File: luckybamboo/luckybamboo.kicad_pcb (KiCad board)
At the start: 4 copper layers, 70.7 x 53.3 mm, 148 parts, among them J1 NEIGHBOR1, J10 TEST_2P, J11 TEST_2P, J12 TEST_2P, J13 TEST_2P, J14 TEST_2P, J15 TEST_2P, J16 TEST_2P, J17 Conn_Coaxial, J18 Conn_Coaxial, J19 TEST_2P, J2 NEIGHBOR2, J20 TEST_2P, J21 TEST_2P, J22 TEST_2P, J23 TEST_2P, J24 TEST_2P, J25 TEST_2P, J26 TEST_2P, J27 TEST_2P, J28 TEST_2P, J29 TEST_2P, J3 Conn_01x08, J30 TEST_2P, J31 TEST_2P, J32 TEST_2P, J33 TEST_2P, J4 Conn_01x08, J5 Conn_01x08, J6 Conn_01x08, J7 BONUS_ROW, J8 TEST_2P, J9 TEST_2P, U1 ADF7242, U10 ADF7242_balun, U11 ADF7242_balun, U12 HHM2293A1, U13 BGA7H1N6, U14 ADF7242_balun, U15 ADF7242_balun, U16 ADF7242_balun, U17 ADF7242_balun, U2 ADF7242, U3 ADF7242, U4 ADF7242, U5 SKY13322, U6 HHM2293A1, U7 HHM2293A1, U8 ADF7242_balun, U9 ADF7242_balun, X1 XTAL4PIN, X2 XTAL4PIN, X3 XTAL4PIN, X4 XTAL4PIN

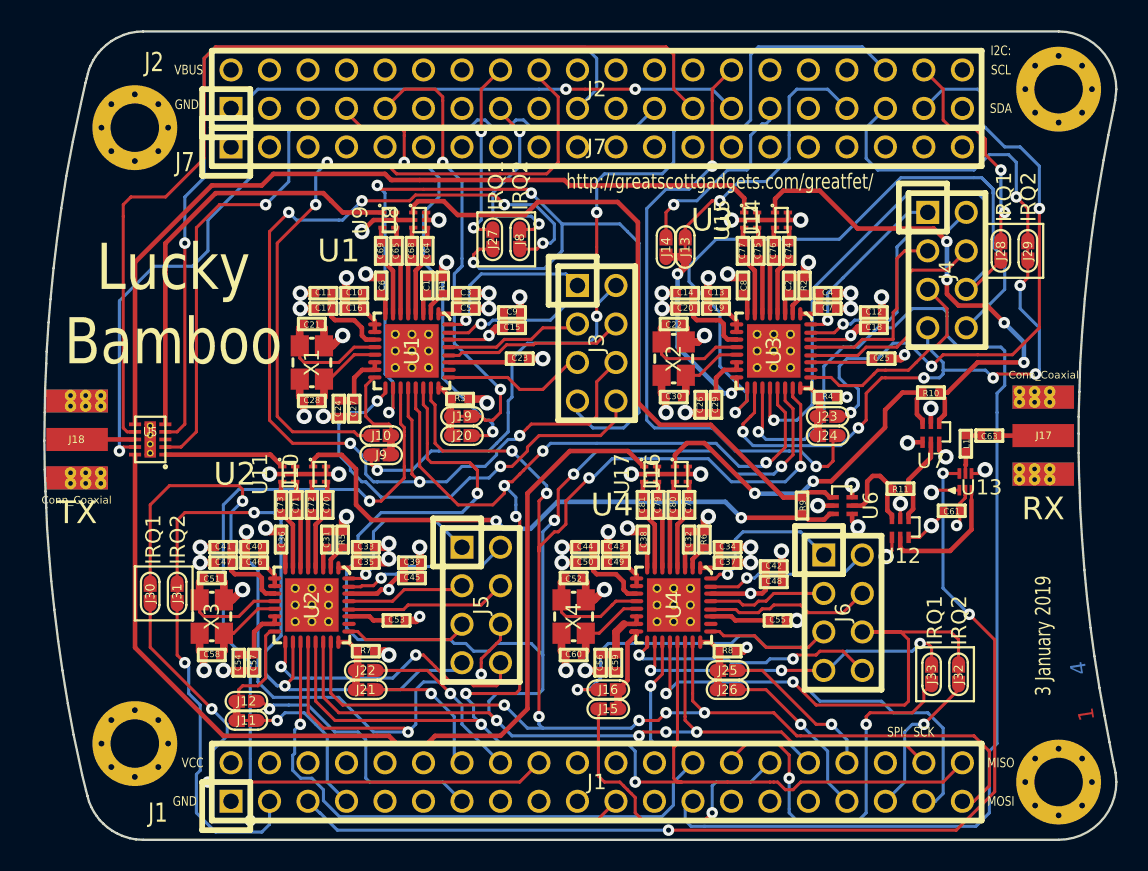
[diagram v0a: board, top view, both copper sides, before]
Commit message: BOM: Changed SMA connectors to RP-SMA and changed SPORT header
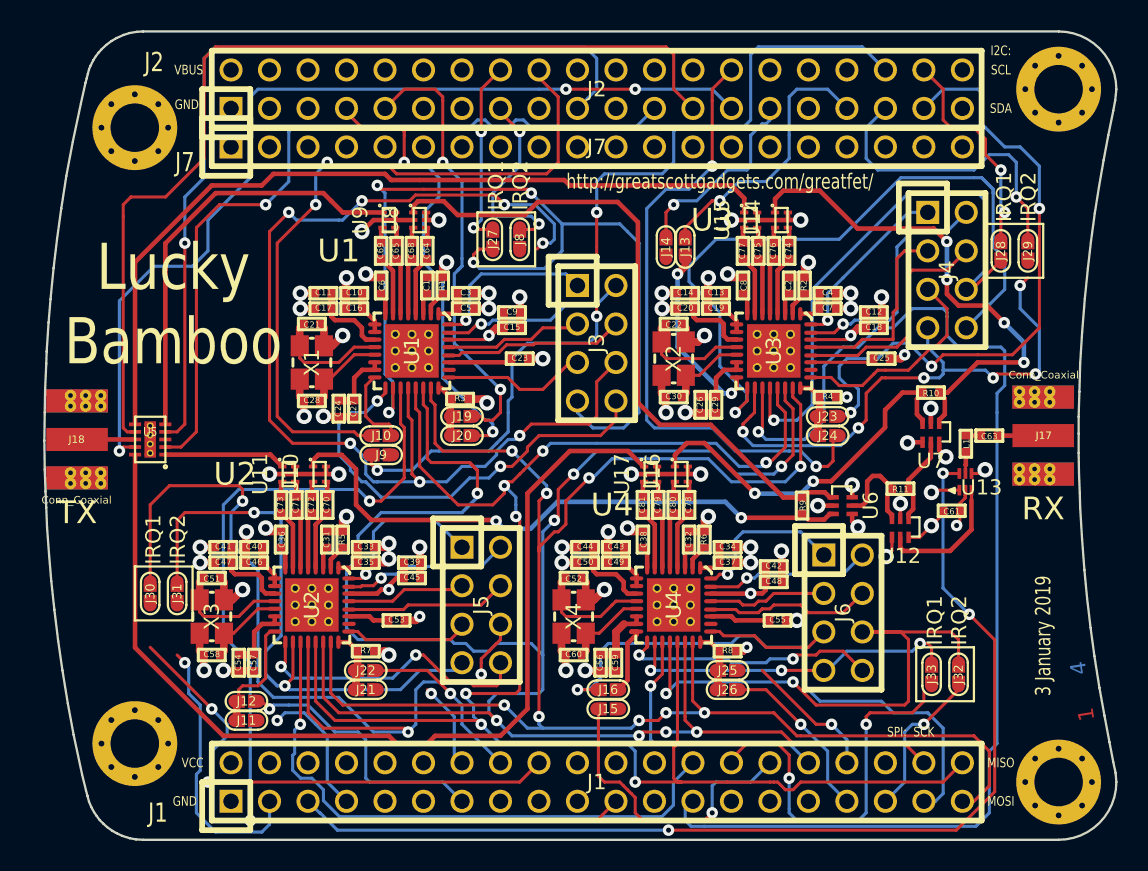
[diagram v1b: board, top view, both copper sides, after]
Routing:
- net /P5_2: track 9.19 -> 5.77 mm
- net /P4_9: track 21.7 -> 18.2 mm
- net /P1_8: track 36.8 -> 33.9 mm
- net /P9_6: track 11.4 -> 9.51 mm
- net /DR3: track 24.1 -> 22.2 mm
- net /P1_0: track 10.9 -> 9.50 mm
- net /~CS~4: track 5.40 -> 4.11 mm
- net /~CS~2: track 5.40 -> 4.11 mm
- net /~CS~3: track 5.49 -> 4.19 mm
- net /~CS~1: track 7.41 -> 6.11 mm
- net /P6_3: track 60.6 -> 59.3 mm
- net /P2_6: track 14.2 -> 12.9 mm
- net /P2_1: track 21.5 -> 20.2 mm
- net /DR2: track 8.99 -> 7.69 mm
- net /DR4: track 5.97 -> 4.70 mm
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
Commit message: Changed  Changed SPI CS 3 and IRQ1 3 pins, which were interfering with SPIFI. Added DC blocking capacitors near TX switch
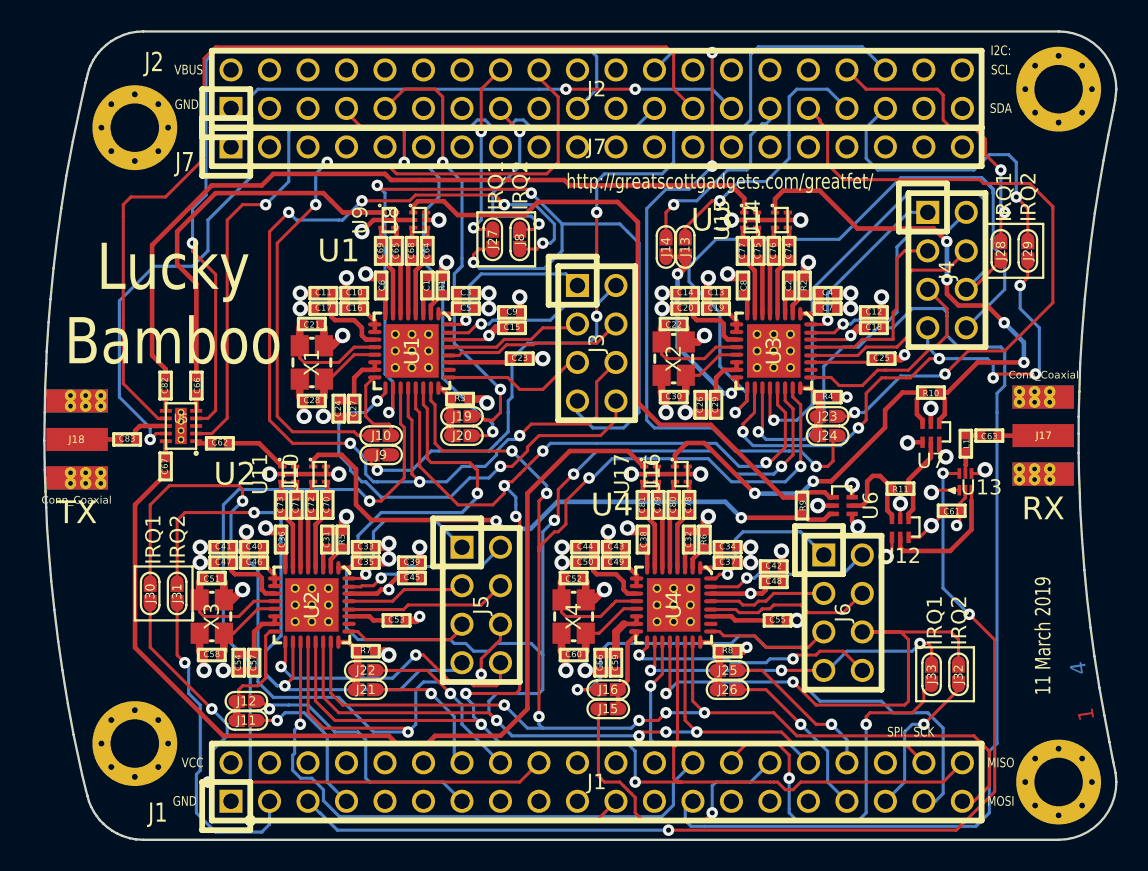
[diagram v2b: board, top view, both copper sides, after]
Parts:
- added C62: 47pF, gsg-modules:0402, F.Cu at (121.2, 95.8)
- added C66: 47pF, gsg-modules:0402, F.Cu at (119.6, 91.9)
- added C67: 47pF, gsg-modules:0402, F.Cu at (117.6, 97.3)
- added C82: 47pF, gsg-modules:0402, F.Cu at (117.6, 91.9)
- added C83: 47pF, gsg-modules:0402, F.Cu at (115.1, 95.5)
- moved U5 2.22 mm to (118.6, 94.6)
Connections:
- J1 pad 10: /P1_1 -> (no net)
- J1 pad 11: /CLK0 -> (no net)
- J1 pad 12: /P1_2 -> (no net)
- J1 pad 15: /P1_7 -> (no net)
- J1 pad 17: /P1_9 -> (no net)
- J1 pad 19: /P5_3 -> (no net)
- J1 pad 20: /P1_10 -> (no net)
- J1 pad 22: /P1_11 -> (no net)
- J1 pad 23: /P5_5 -> (no net)
- J1 pad 24: /P5_4 -> (no net)
- J1 pad 27: /P5_6 -> (no net)
- J1 pad 29: /P5_7 -> (no net)
- J1 pad 31: /P1_18 -> (no net)
- J1 pad 36: /P6_0 -> (no net)
- J1 pad 4: /P0_0 -> (no net)
- J1 pad 6: /P0_1 -> (no net)
- J1 pad 8: /P5_0 -> (no net)
- J1 pad 9: /P5_1 -> (no net)
- J18 pad 1: Net-(J18-Pad1) -> Net-(C83-Pad2)
- J2 pad 10: /P4_6 -> (no net)
- J2 pad 11: /P4_7 -> (no net)
- J2 pad 12: /CLK2 -> (no net)
- J2 pad 13: /P2_8 -> (no net)
- J2 pad 14: /P2_7 -> (no net)
- J2 pad 17: /WAKEUP0 -> (no net)
- J2 pad 2: Net-(J2-Pad2) -> (no net)
- J2 pad 20: /P2_3 -> (no net)
- J2 pad 21: /PF_4 -> (no net)
- J2 pad 22: /P3_2 -> (no net)
- J2 pad 26: /P3_0 -> (no net)
- J2 pad 28: /P3_4 -> (no net)
- J2 pad 3: /P4_8 -> (no net)
- J2 pad 30: /P3_7 -> (no net)
- J2 pad 32: /P3_3 -> (no net)
- J2 pad 37: /P3_5 -> (no net)
- J2 pad 38: /P3_6 -> (no net)
- J2 pad 39: /I2C0_SDA -> (no net)
- J2 pad 4: /P4_0 -> (no net)
- J2 pad 40: /I2C0_SCL -> (no net)
- J2 pad 5: /ADC0_0 -> (no net)
- J2 pad 6: /P4_5 -> (no net)
- J2 pad 8: /P4_2 -> (no net)
- J23 pad 2: /P3_5 -> /P6_7
- J24 pad 2: /P3_4 -> /P3_1
- J28 pad 1: /P3_6 -> /P6_6
- J7 pad 11: /RESET -> (no net)
- J7 pad 12: /VBAT -> (no net)
- J7 pad 13: /P2_11 -> (no net)
- J7 pad 14: /P2_10 -> (no net)
- J7 pad 15: /P6_10 -> (no net)
- J7 pad 16: /P6_9 -> (no net)
- J7 pad 17: /P6_2 -> (no net)
- J7 pad 18: /P6_1 -> (no net)
- J7 pad 2: /P6_4 -> (no net)
- J7 pad 3: /P6_5 -> (no net)
- J7 pad 4: /ADC0_5 -> (no net)
- J7 pad 5: /ADC0_2 -> (no net)
- J7 pad 6: /P2_9 -> (no net)
- J7 pad 7: /P2_12 -> (no net)
- J7 pad 8: /P2_13 -> (no net)
- J7 pad 9: /RTC_ALARM -> (no net)
- U1 pad 26: /RXEN1 -> (no net)
- U2 pad 26: /RXEN2 -> (no net)
- U3 pad 26: /RXEN3 -> (no net)
- U4 pad 26: /RXEN4 -> (no net)
- U5 pad 1: /RFOUT2 -> Net-(C62-Pad2)
- U5 pad 10: /RFOUT4 -> Net-(C67-Pad1)
- U5 pad 3: Net-(U5-Pad3) -> (no net)
- U5 pad 5: /RFOUT1 -> Net-(C66-Pad1)
- U5 pad 6: /RFOUT3 -> Net-(C82-Pad2)
- U5 pad 8: Net-(J18-Pad1) -> Net-(C83-Pad1)
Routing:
- net /P3_1: track 0.00 -> 46.7 mm, vias 0 -> 3
- net /P6_7: track 0.00 -> 43.9 mm, vias 0 -> 2
- net /P3_5: track 42.1 -> 0.00 mm, vias 3 -> 0
- net /P3_4: track 41.7 -> 0.00 mm, vias 2 -> 0
- net /P6_6: track 0.00 -> 19.4 mm, vias 0 -> 2
- net /P3_6: track 14.5 -> 0.00 mm, vias 2 -> 0
- net Net-(J18-Pad1): track 3.83 -> 0.00 mm
- net /RFOUT2: track 8.04 -> 4.22 mm
- net /P5_2: track 5.77 -> 9.19 mm
- net /P4_9: track 18.2 -> 21.7 mm
- net /RFOUT3: track 54.9 -> 51.7 mm
- net /P1_8: track 33.9 -> 36.8 mm
- net /RFOUT1: track 28.2 -> 25.3 mm
- net Net-(C83-Pad2): track 0.00 -> 2.77 mm
- net Net-(C83-Pad1): track 0.00 -> 2.73 mm
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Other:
- board text added: "11 March 2019"
- board text removed: "3 January 2019"

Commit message: Lucky Bamboo: Rerouted RX RF signals and rearranged schematic to be consistent with layout. Gladiolus: Routed incomplete signal near TX transistor.
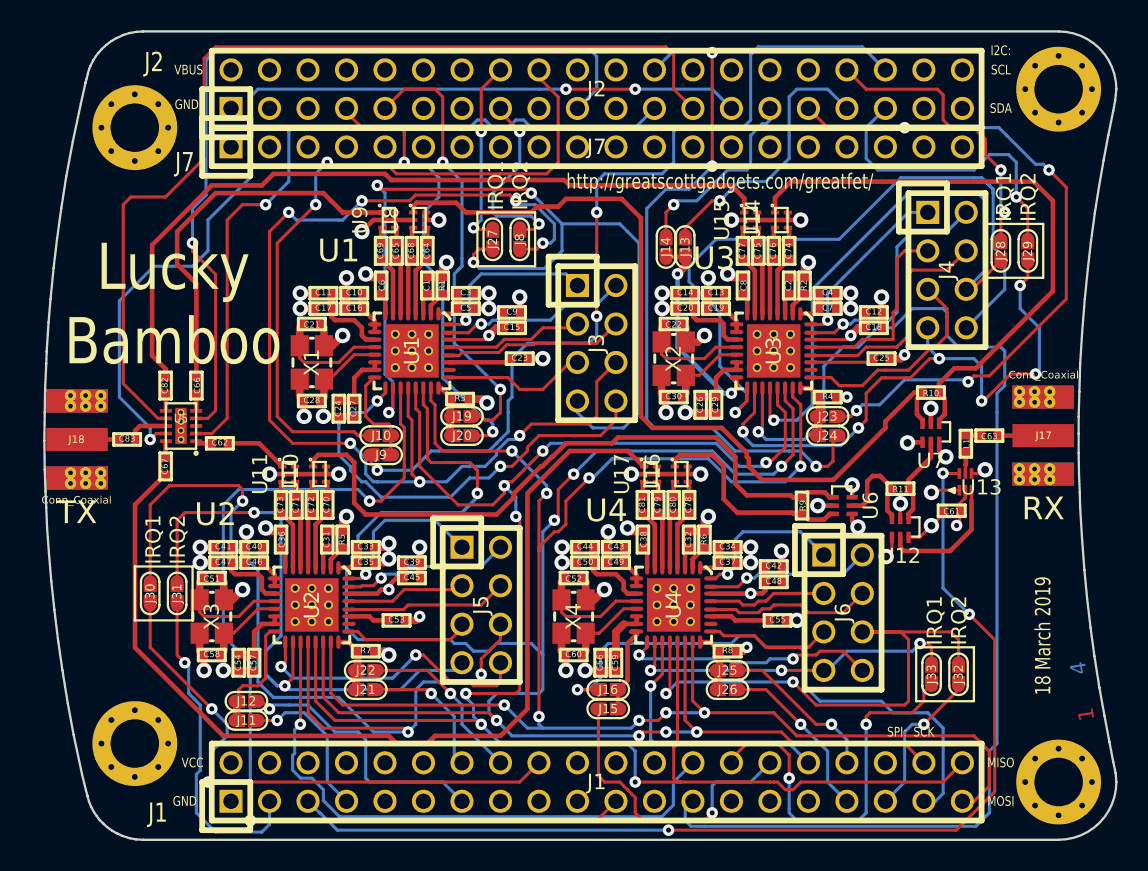
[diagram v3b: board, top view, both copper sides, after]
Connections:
- R10 pad 1: /RFIN4 -> /RFIN1
- R9 pad 1: /RFIN2 -> /RFIN4
- R9 pad 2: /RFIN1 -> /RFIN2
- U6 pad 1: /RFIN1 -> /RFIN2
- U6 pad 3: /RFIN2 -> /RFIN4
- U7 pad 3: /RFIN4 -> /RFIN1
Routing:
- net /RFIN1: track 44.3 -> 55.5 mm
- net /RFIN4: track 24.6 -> 14.2 mm, vias 2 -> 0
- net /RFIN3: track 33.8 -> 39.2 mm, vias 4 -> 0
- net /RFIN2: track 39.9 -> 43.3 mm, vias 2 -> 0
- net /TRFS3: track 38.3 -> 40.4 mm
- net /DR1: track 5.72 -> 6.99 mm
- net /P6_7: track 43.9 -> 45.0 mm, vias 2 -> 4
- net /P4_3: track 29.6 -> 30.2 mm
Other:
- board text added: "18 March 2019"
- board text removed: "11 March 2019"

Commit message: Replaced rescued symbols on Gladiolus and Lucky Bamboo. Lucky Bamboo: Shorted IRQ1/IRQ2 jumpers to create default connections.
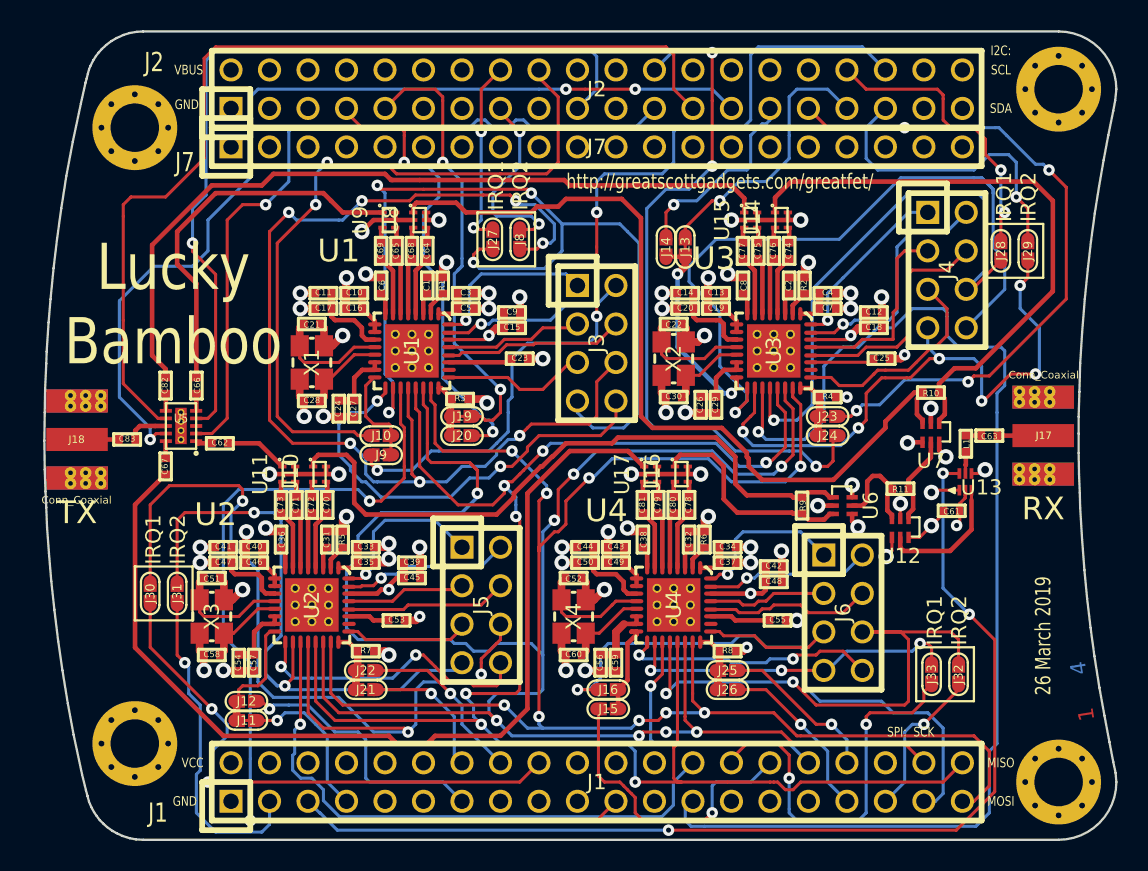
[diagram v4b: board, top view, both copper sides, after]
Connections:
- J1 pad 30: /P1_16 -> /DR4
- J1 pad 7: /P1_0 -> /DR2
- J11 pad 2: /P1_0 -> /DR2
- J13 pad 2: /P2_2 -> /DR3
- J15 pad 2: /P1_16 -> /DR4
- J19 pad 1: /~CS~1 -> /P4_3
- J2 pad 33: /P2_2 -> /DR3
- J2 pad 36: /P6_3 -> /DR1
- J20 pad 1: /~CS~1 -> /P4_3
- J21 pad 1: /~CS~2 -> /P5_2
- J22 pad 1: /~CS~2 -> /P5_2
- J23 pad 1: /~CS~3 -> /P6_7
- J24 pad 1: /~CS~3 -> /P6_7
- J25 pad 1: /~CS~4 -> /P9_6
- J26 pad 1: /~CS~4 -> /P9_6
- J9 pad 2: /P6_3 -> /DR1
- R3 pad 2: /~CS~1 -> /P4_3
- R4 pad 2: /~CS~3 -> /P6_7
- R7 pad 2: /~CS~2 -> /P5_2
- R8 pad 2: /~CS~4 -> /P9_6
- U1 pad 24: /~CS~1 -> /P4_3
- U2 pad 24: /~CS~2 -> /P5_2
- U3 pad 24: /~CS~3 -> /P6_7
- U4 pad 24: /~CS~4 -> /P9_6
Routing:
- net /DR1: track 6.99 -> 67.5 mm, vias 0 -> 3
- net /P6_3: track 59.3 -> 0.00 mm, vias 3 -> 0
- net /DR4: track 6.09 -> 28.3 mm, vias 0 -> 1
- net /P1_16: track 20.9 -> 0.00 mm, vias 1 -> 0
- net /DR3: track 24.1 -> 43.4 mm, vias 2 -> 3
- net /P2_2: track 18.0 -> 0.00 mm, vias 1 -> 0
- net /DR2: track 7.69 -> 19.6 mm, vias 0 -> 1
- net /P1_0: track 10.9 -> 0.00 mm, vias 1 -> 0
- net /P4_3: track 30.2 -> 37.6 mm
- net /~CS~1: track 6.11 -> 0.00 mm
- net /P6_7: track 45.0 -> 50.4 mm
- net /P9_6: track 11.2 -> 16.6 mm
- net /P5_2: track 9.19 -> 14.6 mm
- net /~CS~3: track 4.19 -> 0.00 mm
- net /~CS~4: track 4.11 -> 0.00 mm
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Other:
- board text added: "26 March 2019"
- board text removed: "18 March 2019"
